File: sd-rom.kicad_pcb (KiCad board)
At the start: 2 copper layers, 100 x 100 mm, 4 parts, among them J1 JAE50, J2 Conn_01x40, J3 Conn_01x40, J4 SD44

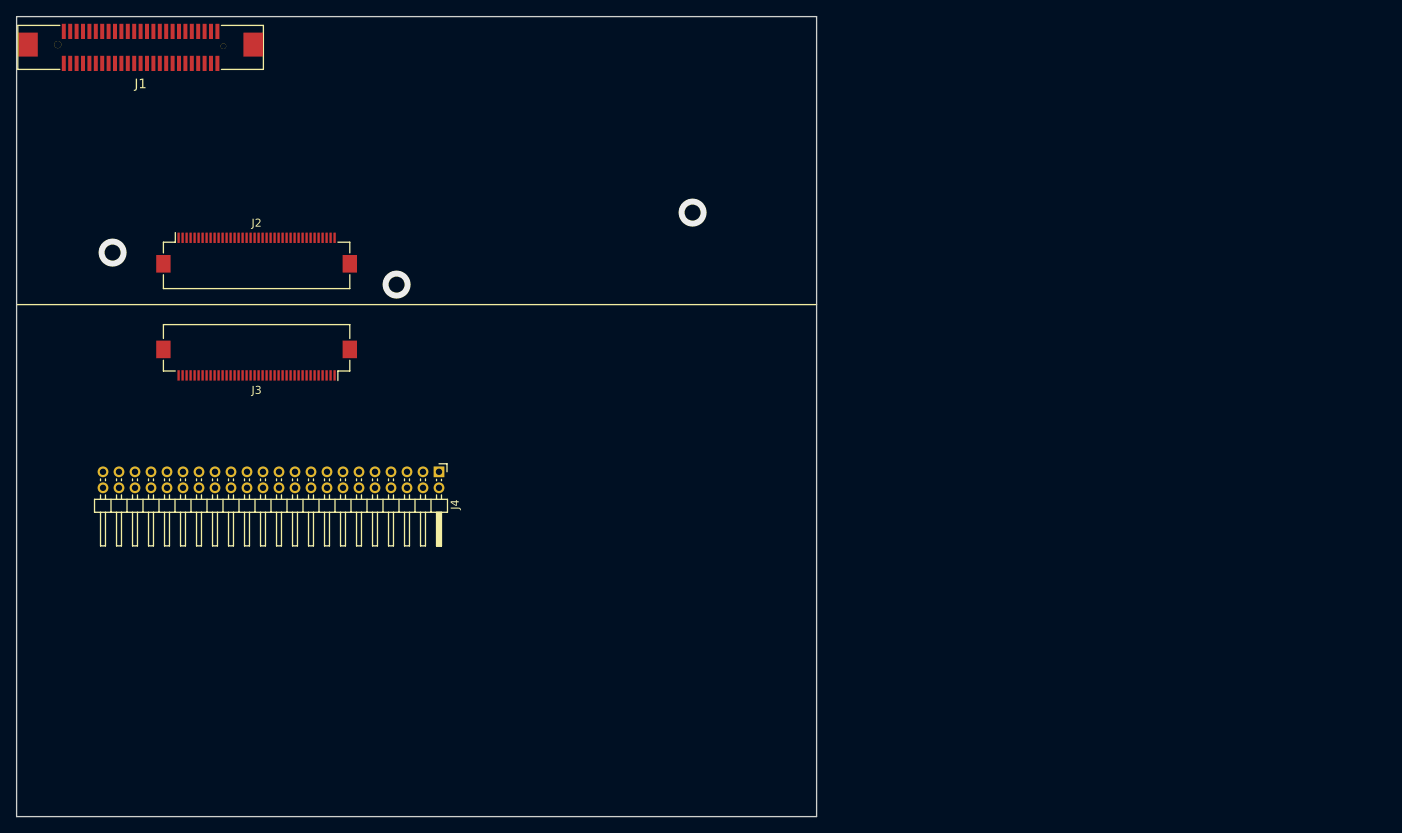
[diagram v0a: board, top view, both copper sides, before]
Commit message: second board dimensions
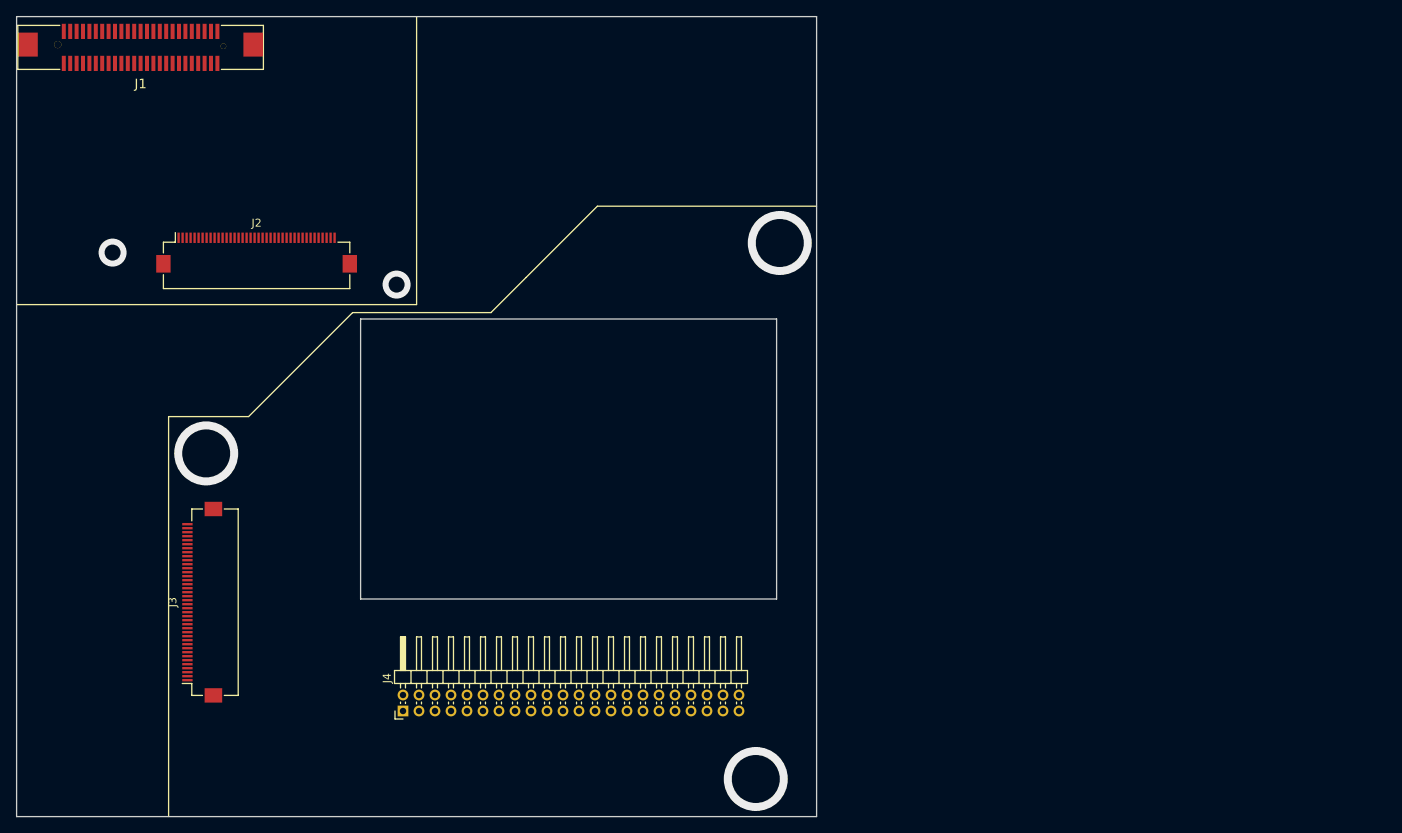
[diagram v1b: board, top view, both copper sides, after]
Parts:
- moved J3 31.0 mm to (23.2, 73.2), turned to 90 degrees
- moved J4 30.2 mm to (48.3, 86.8), turned to 90 degrees
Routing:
- net GNDREF: vias 3 -> 2
- net (no net): vias 0 -> 3
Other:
- outline, holes or cut-outs redrawn

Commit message: board variant 1
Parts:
- moved J1 123.6 mm to (146.9, 25.8)
- moved J2 123.2 mm to (151.1, 52.1)
- moved J4 23.7 mm to (48.3, 63.1)
- moved J3 14.1 mm to (32.9, 62.9), turned to 315 degrees
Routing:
- net GNDREF: vias 2 -> 1
- net (no net): vias 3 -> 4
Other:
- board size 100 x 100 mm -> 171.1 x 100 mm

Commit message: board variant 2
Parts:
- J1, J2: moved to B.Cu
- moved J3 52.6 mm to (75.4, 93.9), turned to 0 degrees
- moved J4 20.5 mm to (58.0, 81.2), turned to 135 degrees
- moved J2 12.8 mm to (139.8, 46.1), turned to 180 degrees
- moved J1 7.44 mm to (143.2, 19.4), turned to 180 degrees
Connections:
- J1 pad : GNDREF -> (no net)
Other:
- board size 171.1 x 100 mm -> 157.8 x 100 mm

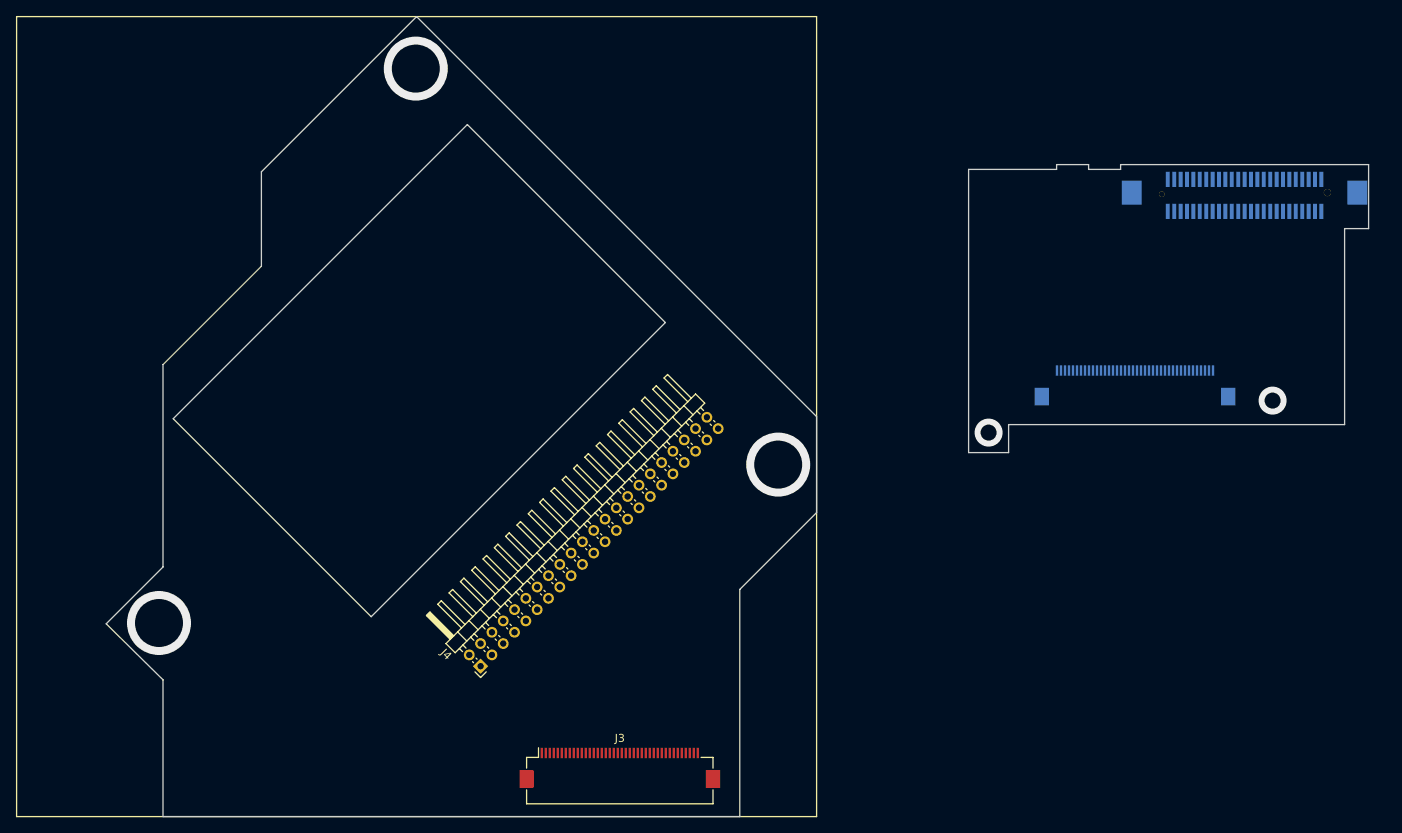
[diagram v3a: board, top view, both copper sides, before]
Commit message: attiny added to schema
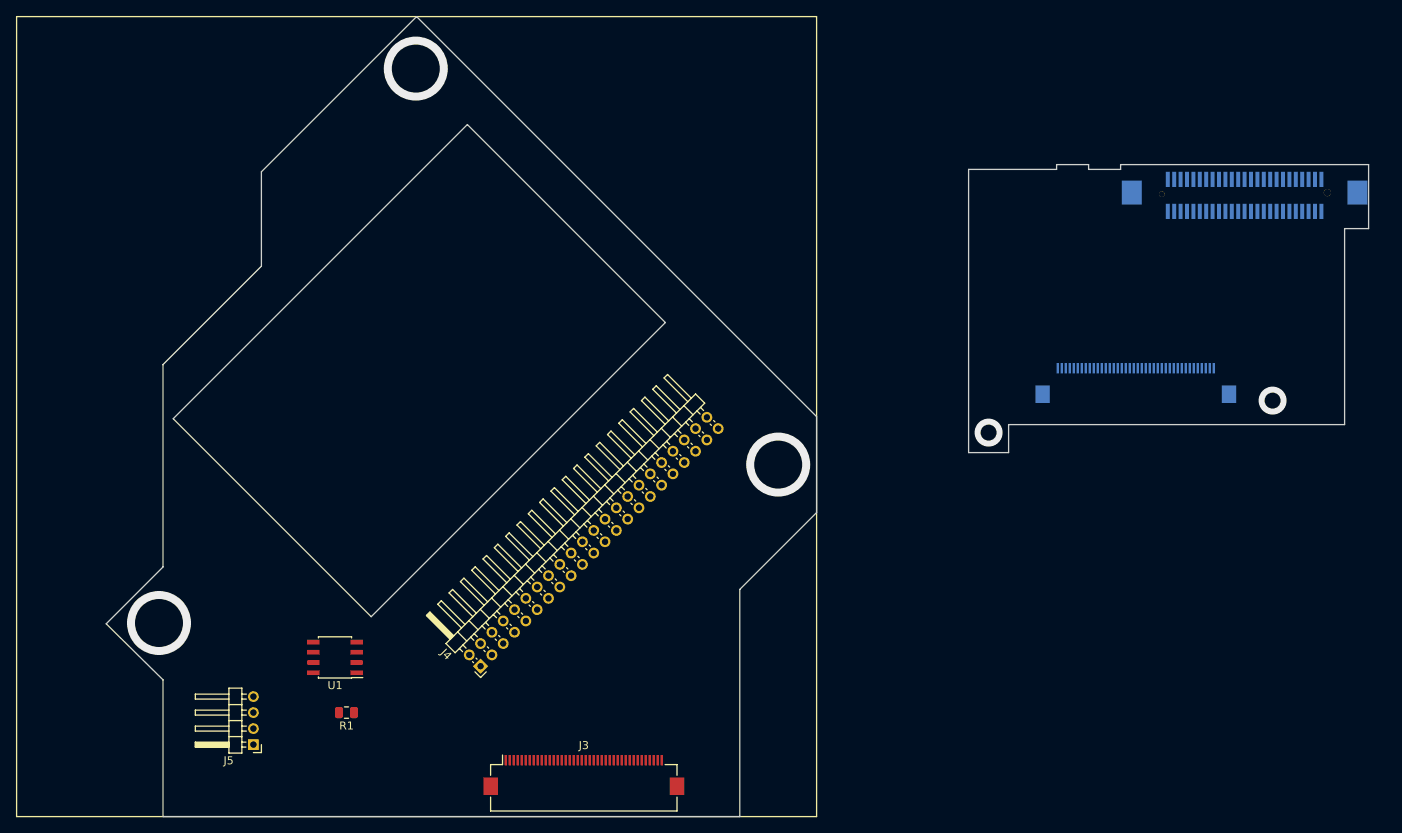
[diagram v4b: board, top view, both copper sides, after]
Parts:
- added J5: Conn_01x04_Male, sd-rom:PinHeader_1x04_P2.00mm_Horizontal, F.Cu at (29.6, 91.0)
- added R1: 300, sd-rom:R_0805_2012Metric, F.Cu at (41.2, 87.0)
- added U1: ATtiny13A-SSU, sd-rom:SOIC-8_3.9x4.9mm_P1.27mm, F.Cu at (39.8, 80.1)
- moved J3 4.59 mm to (70.9, 94.8)
- moved J2 0.32 mm to (139.9, 45.8)
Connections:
- net Net-(J3-Pad20) renamed VCC

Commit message: schema update
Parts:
- added C1: 10, sd-rom:C_0805_2012Metric, F.Cu at (34.0, 86.0)
- added C2: 100, sd-rom:C_0805_2012Metric, F.Cu at (34.0, 74.0)
- added R2: 0, sd-rom:R_0805_2012Metric, F.Cu at (130.8, 34.0)
- added R3: 300, sd-rom:R_0805_2012Metric, F.Cu at (41.0, 80.0)
- added U2: AMS1117-3.3, sd-rom:SOT-223-3_TabPin2, F.Cu at (34.0, 93.3)
- moved J5 25.2 mm to (26.6, 66.0)
- moved R1 15.9 mm to (27.0, 80.0), turned to 270 degrees
- moved U1 5.80 mm to (34.0, 80.0)
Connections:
- net Net-(J5-Pad4) renamed /Button
- J2 pad 39: Net-(J1-Pad37) -> Net-(J2-Pad39)
- J3 pad 39: Net-(J3-Pad39) -> /LedIn
- J4 pad 39: Net-(J3-Pad39) -> /LedIn
- R1 pad 1: Net-(R1-Pad1) -> Net-(J5-Pad3)
- R1 pad 2: Net-(J5-Pad3) -> /LedOut
- U1 pad 2: Net-(J5-Pad1) -> /Motor
- U1 pad 6: Net-(U1-Pad6) -> /LedOut
- U1 pad 7: Net-(U1-Pad7) -> /LedIn
- U1 pad 8: VCC -> Net-(C2-Pad1)

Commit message: schema fix
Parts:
- R2: moved to B.Cu
- moved R1 14.0 mm to (41.0, 79.0)
- moved R3 14.0 mm to (27.0, 79.0)
- moved R2 1.25 mm to (130.0, 33.0)
- moved C1 1.00 mm to (34.0, 85.0)
- moved C2 1.00 mm to (34.0, 73.0), turned to 180 degrees
- moved U1 1.00 mm to (34.0, 79.0), turned to 0 degrees
- moved U2 0.30 mm to (34.0, 93.0)
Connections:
- U1 pad 5: /Button -> /LedOut
- U1 pad 6: /LedOut -> /Button
